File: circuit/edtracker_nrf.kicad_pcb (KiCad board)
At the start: 2 copper layers, 42.7 x 34 mm, 17 parts, among them M1 NRF24LE1_SMALL, Q1 TPS1101D, SW1 SW_PUSH, SW2 SWITCH_INV, U1 NRF24LE1_PROG, U2 MPU-6050, U3 UART

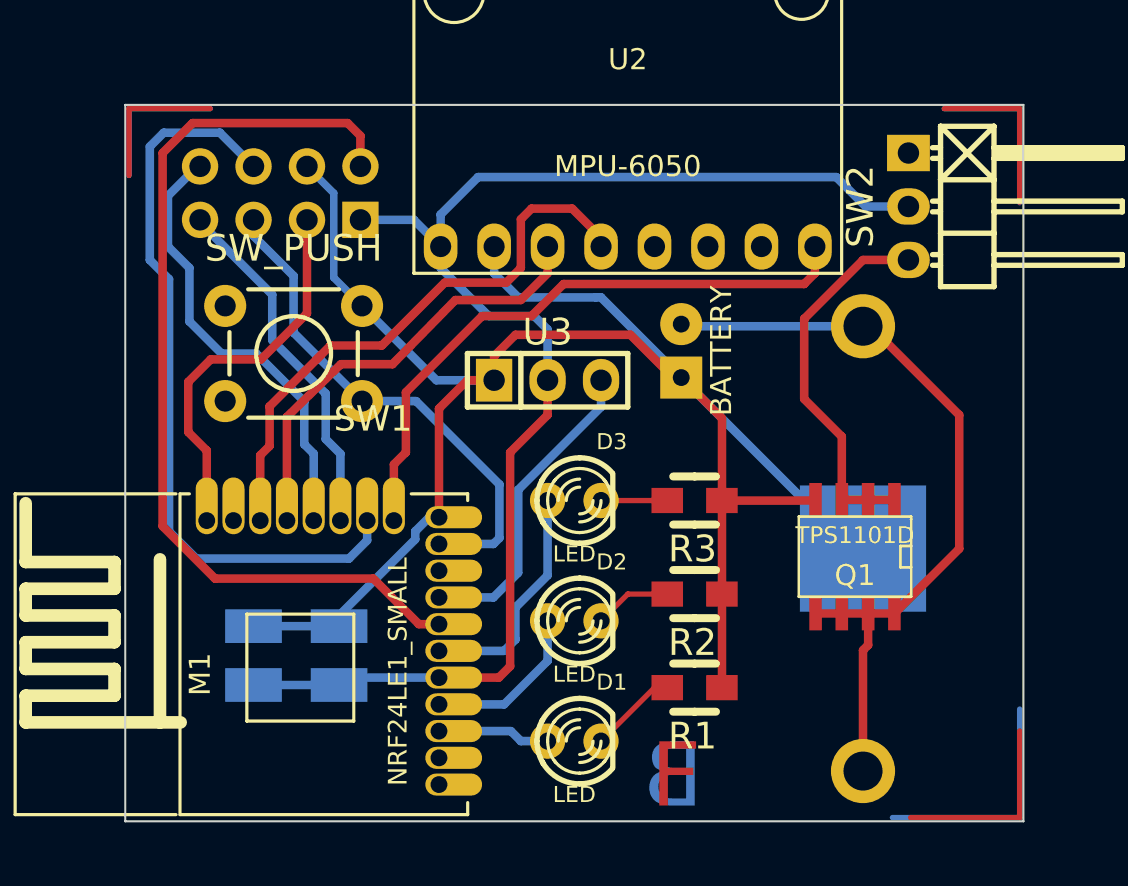
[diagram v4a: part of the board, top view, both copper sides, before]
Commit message: 
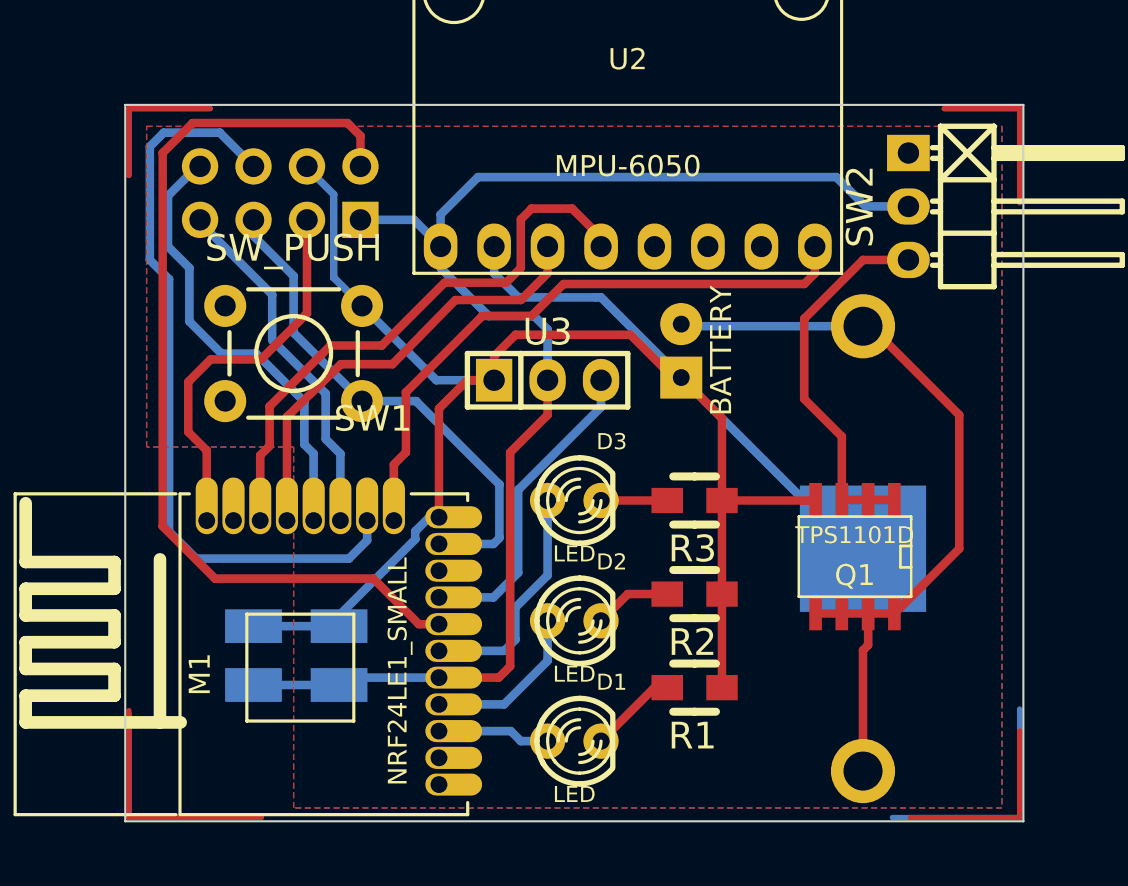
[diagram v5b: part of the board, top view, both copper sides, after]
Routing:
- net (no net): track 50.6 -> 73.0 mm
- net GND: track 94.7 -> 93.9 mm
- added copper zone on B.Cu, net GND
- added copper zone on F.Cu, net GND
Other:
- board text removed: "B"
- board text removed: "F"
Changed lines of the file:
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@@
     (links 46)
     (no_connects 2)
-    (area 138.255599 85.394799 191.465201 127.2286)
+    (area 138.255599 85.394799 191.465201 127.050001)
     (thickness 1.6)
-    (drawings 6)
-    (tracks 193)
+    (drawings 4)
+    (tracks 197)
     (zones 0)
     (modules 17)
@@
     (visible_elements 7FFFFFFF)
     (pcbplotparams
-      (layerselection 32769)
+      (layerselection 271613953)
       (usegerberextensions true)
       (excludeedgelayer true)
@@
       (drillshape 0)
       (scaleselection 1)
-      (outputdirectory ""))
+      (outputdirectory gerbers/))
   )
   (net 0 "")
@@
     )
   )
-  (gr_text F (at 169.926 124.841) (layer F.Cu)
-    (effects (font (size 3.048 3.048) (thickness 0.508)))
-  )
-  (gr_text B (at 169.799 124.841) (layer B.Cu)
-    (effects (font (size 3.048 3.048) (thickness 0.508)) (justify mirror))
-  )
   (gr_line (start 143.764 92.964) (end 143.764 127) (angle 90) (layer Edge.Cuts) (width 0.1))
   (gr_line (start 186.436 92.964) (end 143.764 92.964) (angle 90) (layer Edge.Cuts) (width 0.1))
   (gr_line (start 186.436 127) (end 186.436 92.964) (angle 90) (layer Edge.Cuts) (width 0.1))
   (gr_line (start 143.764 127) (end 186.436 127) (angle 90) (layer Edge.Cuts) (width 0.1))
+  (segment (start 143.9418 121.7422) (end 143.9418 126.8222) (width 0.254) (layer F.Cu) (net 0))
+  (segment (start 143.9418 126.8222) (end 150.241 126.8222) (width 0.254) (layer F.Cu) (net 0))
+  (segment (start 143.9418 121.9454) (end 143.9418 126.8222) (width 0.254) (layer B.Cu) (net 0))
+  (segment (start 143.9418 126.8222) (end 150.0632 126.8222) (width 0.254) (layer B.Cu) (net 0))
   (segment (start 186.2582 121.666) (end 186.2582 126.8222) (width 0.254) (layer B.Cu) (net 0))
   (segment (start 186.2582 126.8222) (end 180.213 126.8222) (width 0.254) (layer B.Cu) (net 0))
@@
   (segment (start 178.308 114.046) (end 170.18 105.918) (width 0.4064) (layer B.Cu) (net 1))
   (segment (start 181.61 114.935) (end 179.07 114.935) (width 0.4064) (layer B.Cu) (net 1) (status 30))
-  (segment (start 155.0162 102.5144) (end 155.0162 101.7397) (width 0.3556) (layer F.Cu) (net 1))
   (segment (start 161.29 106.045) (end 158.5468 106.045) (width 0.4064) (layer B.Cu) (net 1))
   (segment (start 158.5468 106.045) (end 155.0162 102.5144) (width 0.4064) (layer B.Cu) (net 1))
@@
   (segment (start 158.21025 112.55375) (end 158.670625 112.55375) (width 0.4064) (layer B.Cu) (net 1))
   (segment (start 161.29 99.695) (end 161.29 99.06) (width 0.3048) (layer B.Cu) (net 1))
-  (segment (start 153.67 97.155) (end 153.67 101.1682) (width 0.3556) (layer B.Cu) (net 1))
   (segment (start 153.67 101.1682) (end 155.0162 102.5144) (width 0.3556) (layer B.Cu) (net 1))
-  (segment (start 152.4 95.885) (end 153.67 97.155) (width 0.3556) (layer B.Cu) (net 1))
+  (segment (start 153.67 97.2185) (end 153.67 101.1682) (width 0.3556) (layer B.Cu) (net 1))
+  (segment (start 152.4 95.9485) (end 153.67 97.2185) (width 0.3556) (layer B.Cu) (net 1))
+  (segment (start 152.4 95.885) (end 152.4 95.9485) (width 0.3556) (layer B.Cu) (net 1))
   (segment (start 178.816 103.4796) (end 179.1716 103.4796) (width 0.4064) (layer F.Cu) (net 2))
   (segment (start 179.1716 103.4796) (end 183.388 107.696) (width 0.4064) (layer F.Cu) (net 2))
@@
   (segment (start 162.08375 122.71375) (end 158.670625 122.71375) (width 0.4064) (layer B.Cu) (net 4))
   (segment (start 162.56 123.19) (end 162.08375 122.71375) (width 0.4064) (layer B.Cu) (net 4))
-  (segment (start 168.91 120.65) (end 166.37 123.19) (width 0.254) (layer F.Cu) (net 5))
+  (segment (start 168.91 120.65) (end 166.37 123.19) (width 0.4064) (layer F.Cu) (net 5))
   (segment (start 169.51452 120.65) (end 168.91 120.65) (width 0.254) (layer F.Cu) (net 5))
   (segment (start 163.83 117.475) (end 163.83 119.38) (width 0.4064) (layer B.Cu) (net 6))
   (segment (start 161.76625 121.44375) (end 158.670625 121.44375) (width 0.4064) (layer B.Cu) (net 6))
   (segment (start 163.83 119.38) (end 161.76625 121.44375) (width 0.4064) (layer B.Cu) (net 6))
-  (segment (start 167.64 116.205) (end 166.37 117.475) (width 0.254) (layer F.Cu) (net 7))
-  (segment (start 169.51452 116.205) (end 167.64 116.205) (width 0.254) (layer F.Cu) (net 7))
+  (segment (start 167.64 116.205) (end 166.37 117.475) (width 0.4064) (layer F.Cu) (net 7))
+  (segment (start 169.51452 116.205) (end 167.64 116.205) (width 0.4064) (layer F.Cu) (net 7))
   (segment (start 163.83 111.76) (end 163.83 115.316) (width 0.4064) (layer B.Cu) (net 8))
   (segment (start 161.76625 118.90375) (end 158.670625 118.90375) (width 0.4064) (layer B.Cu) (net 8))
@@
   (segment (start 162.306 116.84) (end 162.306 118.364) (width 0.4064) (layer B.Cu) (net 8))
   (segment (start 163.83 115.316) (end 162.306 116.84) (width 0.4064) (layer B.Cu) (net 8))
-  (segment (start 166.37 111.76) (end 169.51452 111.76) (width 0.254) (layer F.Cu) (net 9))
+  (segment (start 166.37 111.76) (end 169.51452 111.76) (width 0.4064) (layer F.Cu) (net 9))
   (segment (start 154.94 95.885) (end 154.94 94.4372) (width 0.4064) (layer F.Cu) (net 10))
   (segment (start 157.71495 117.63375) (end 158.670625 117.63375) (width 0.4064) (layer F.Cu) (net 10))
@@
   (segment (start 153.289 108.839) (end 153.9875 109.5375) (width 0.4064) (layer B.Cu) (net 20))
   (segment (start 153.9875 109.5375) (end 153.9875 112.7125) (width 0.4064) (layer B.Cu) (net 20))
+  (zone (net 1) (net_name GND) (layer B.Cu) (hatch edge 0.508)
+    (connect_pads (clearance 0.508))
+    (min_thickness 0.508)
+    (fill yes (arc_segments 16) (thermal_gap 0.508) (thermal_bridge_width 1.016))
+    (polygon
+      (pts
+        (xy 144.78 93.98) (xy 185.42 93.98) (xy 185.42 126.365) (xy 151.765 126.365) (xy 151.765 109.22)
+        (xy 144.78 109.22)
+      )
+    )
+  )
+  (zone (net 1) (net_name GND) (layer F.Cu) (hatch edge 0.508)
+    (connect_pads (clearance 0.508))
+    (min_thickness 0.508)
+    (fill yes (arc_segments 16) (thermal_gap 0.508) (thermal_bridge_width 1.016))
+    (polygon
+      (pts
+        (xy 144.78 93.98) (xy 185.42 93.98) (xy 185.42 126.365) (xy 151.765 126.365) (xy 151.765 109.22)
+        (xy 144.78 109.22)
+      )
+    )
+  )
 )

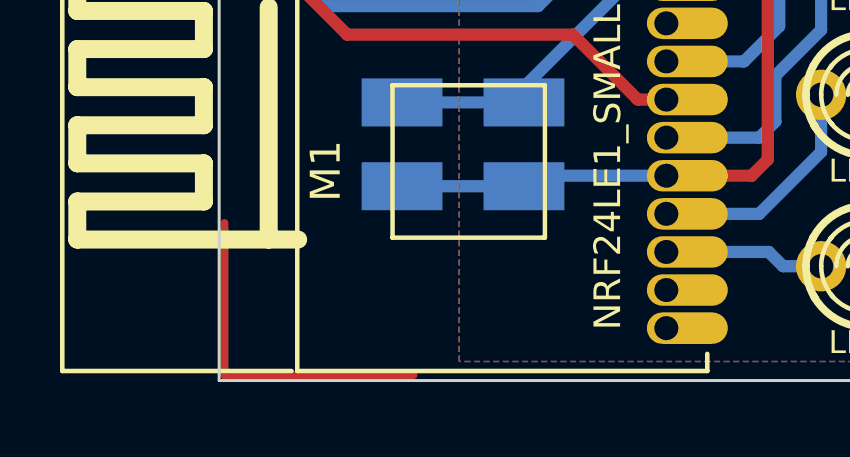
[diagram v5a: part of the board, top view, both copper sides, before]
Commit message: 
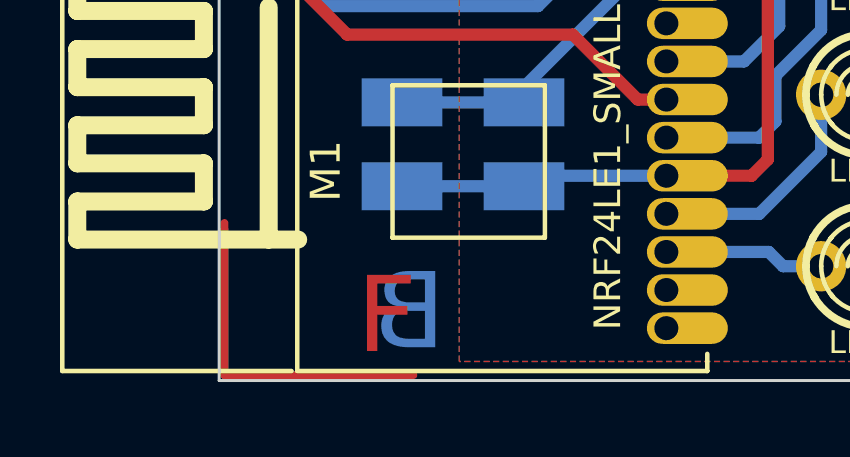
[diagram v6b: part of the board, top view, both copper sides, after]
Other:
- board text added: "B"
- board text added: "F"

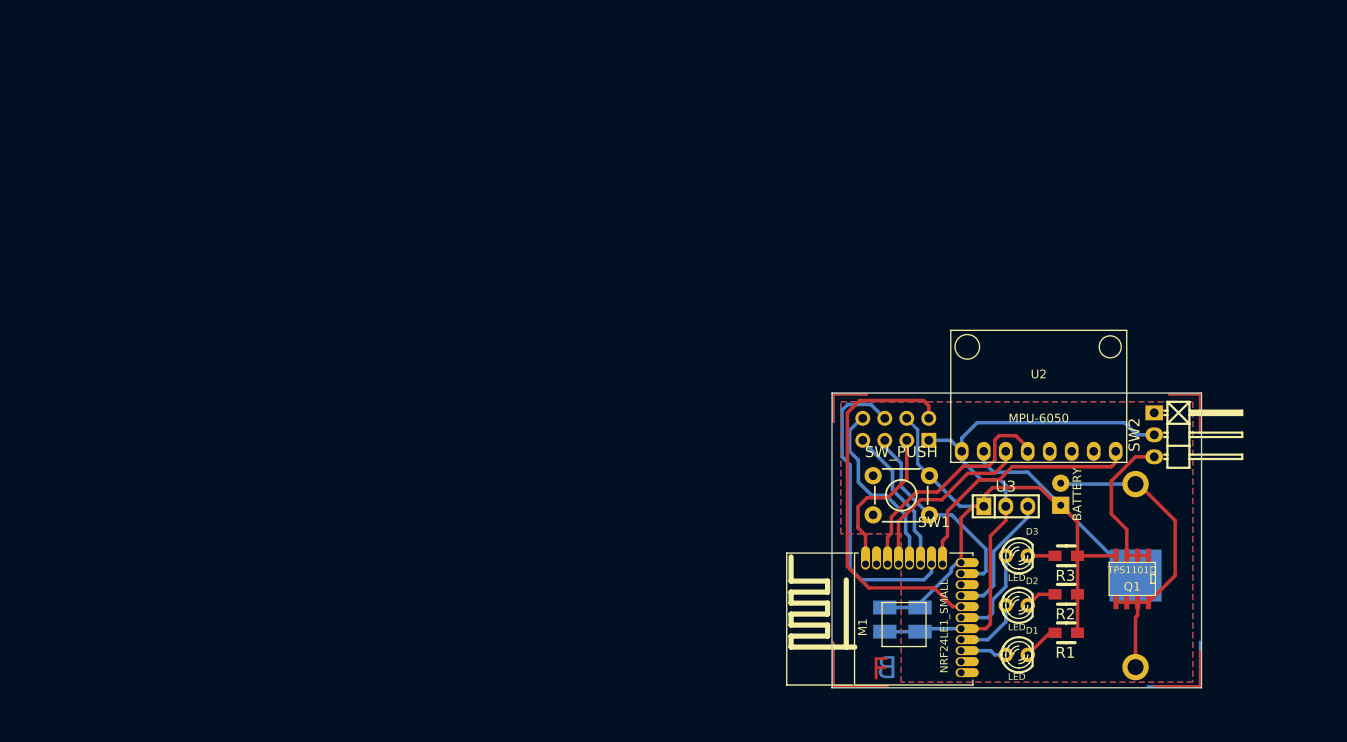
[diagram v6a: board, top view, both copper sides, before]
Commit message: 
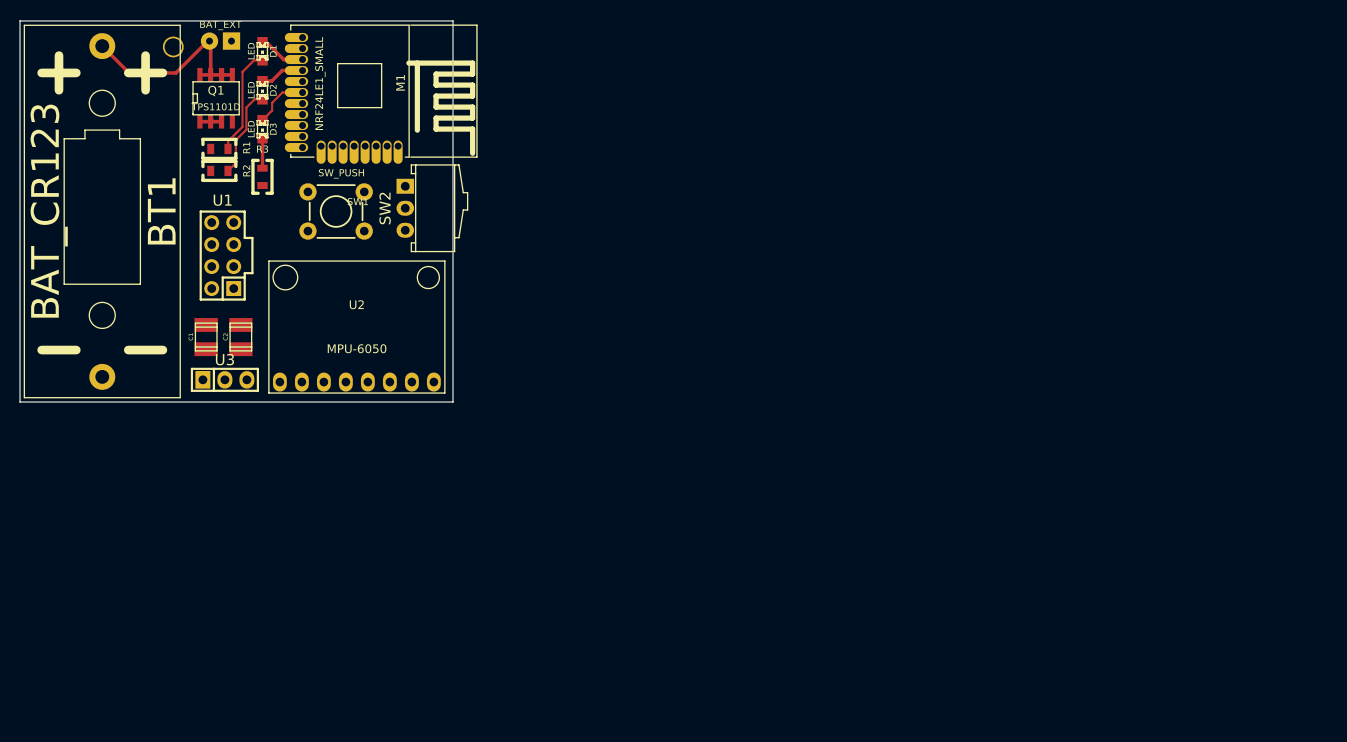
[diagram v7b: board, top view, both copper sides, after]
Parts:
- BT1: value BATTERY_CR2032 -> BAT_CR123; footprint edtracker_nrf:CR2032_THT -> edtracker_nrf:CR123; moved to F.Cu
- BT2: value BATTERY -> BAT_EXT
- C1, C2: moved to F.Cu
- D1, D2, D3: footprint LEDs:LED-3MM -> LEDs:LED-0805
- R1, R2, R3: footprint Resistors_SMD:Resistor_SMD0805_HandSoldering -> Resistors_SMD:Resistor_SMD0805_ReflowWave
- SW2: footprint Pin_Headers:Pin_Header_Angled_1x03 -> edtracker_nrf:ESP2010_switch
- U1: footprint edtracker_nrf:Pin_Header_Angled_2x04 -> edtracker_nrf:Pin_Header_Straight_2x04; moved to F.Cu
- moved BT1 126.5 mm to (59.5, 72.0), turned to 0 degrees
- moved Q1 119.5 mm to (72.6, 58.9), turned to 0 degrees
- moved R1 112.6 mm to (73.0, 64.8), turned to 0 degrees
- moved D1 111.5 mm to (78.0, 53.5), turned to 270 degrees
- moved BT2 110.2 mm to (73.2, 52.3), turned to 0 degrees
- moved R2 109.3 mm to (73.0, 67.3), turned to 0 degrees
- moved D2 105.5 mm to (78.0, 58.0), turned to 270 degrees
- moved R3 102.6 mm to (78.0, 68.0), turned to 90 degrees
- moved D3 100.1 mm to (78.0, 62.5), turned to 270 degrees
- moved U3 91.3 mm to (73.7, 91.4)
- moved SW2 90.4 mm to (94.5, 71.6)
- moved M1 88.5 mm to (88.3, 58.4), turned to 270 degrees
- moved C2 84.9 mm to (75.5, 86.5), turned to 90 degrees
- moved C1 84.9 mm to (71.5, 86.5), turned to 90 degrees
- moved U1 80.3 mm to (73.4, 77.1), turned to 90 degrees
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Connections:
- BT1 pad 1: Net-(BT1-Pad0) -> Net-(BT1-Pad1)
- BT2 pad 1: Net-(BT1-Pad0) -> Net-(BT1-Pad1)
- Q1 pad 5: Net-(BT1-Pad0) -> Net-(BT1-Pad1)
- Q1 pad 6: Net-(BT1-Pad0) -> Net-(BT1-Pad1)
- Q1 pad 7: Net-(BT1-Pad0) -> Net-(BT1-Pad1)
- Q1 pad 8: Net-(BT1-Pad0) -> Net-(BT1-Pad1)
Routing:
- net GND: track 93.9 -> 0.00 mm
- net (no net): track 73.0 -> 0.00 mm
- net VCC: track 66.0 -> 0.00 mm
- net Net-(M1-Pad7): track 44.5 -> 0.00 mm
- net Net-(BT1-Pad0): track 37.0 -> 0.00 mm
- net /FMOSI: track 35.8 -> 0.00 mm
- net Net-(M1-Pad12): track 29.4 -> 0.00 mm
- net /SDA: track 27.6 -> 0.00 mm
- net /FSCK: track 24.4 -> 0.00 mm
- net Net-(BT1-Pad1): track 0.00 -> 22.9 mm
- net /SCL: track 22.0 -> 0.00 mm
- net /FCSN: track 21.4 -> 0.00 mm
- net Net-(M1-Pad19): track 18.4 -> 0.00 mm
- net /FMISO: track 17.0 -> 0.00 mm
- net Net-(Q1-Pad1): track 18.5 -> 2.50 mm
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- removed copper zone on B.Cu, net GND
- removed copper zone on F.Cu, net GND
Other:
- board size 42.7 x 34 mm -> 50 x 44 mm
- board text removed: "B"
- board text removed: "F"
